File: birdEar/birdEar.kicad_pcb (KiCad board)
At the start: 2 copper layers, 96.5 x 88.9 mm, 59 parts, among them J1 Conn_01x03, J2 Micro_SD_Card_Det_Hirose_DM3AT, J3 SWD, J4 Conn_01x02_Male, J5 Conn_01x08_Male, J6 Conn_01x03_Male, SW2 KSA0A311 LFTR, SW3 KSA0A311 LFTR, SW4 KSA0A311 LFTR, U1 LM324, U2 AZ1117EH-3.3TRG1, U3 STM32F746ZGTx, U4 Si7050-A20, U5 LTR-303ALS-01

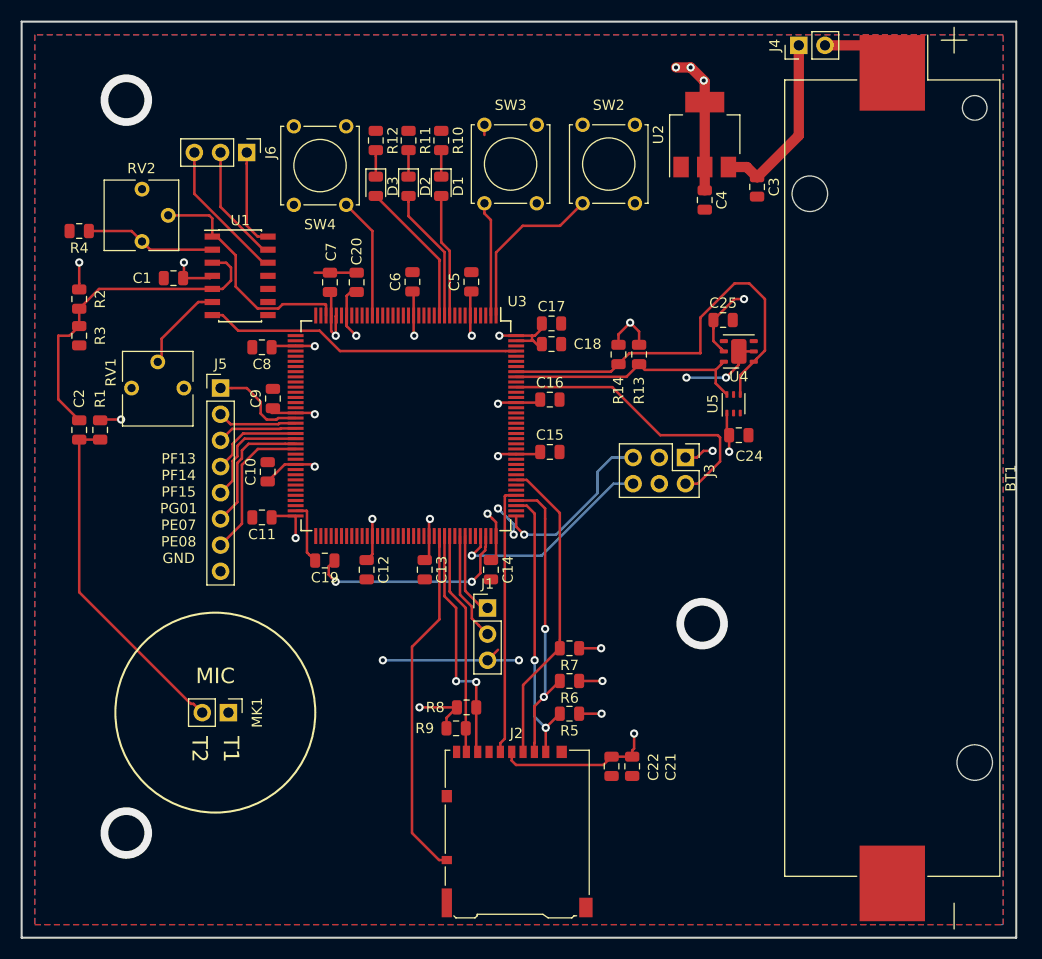
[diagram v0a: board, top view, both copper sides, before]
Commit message: Implemented anti aliasing filter, worked on the layout, added some gnd points
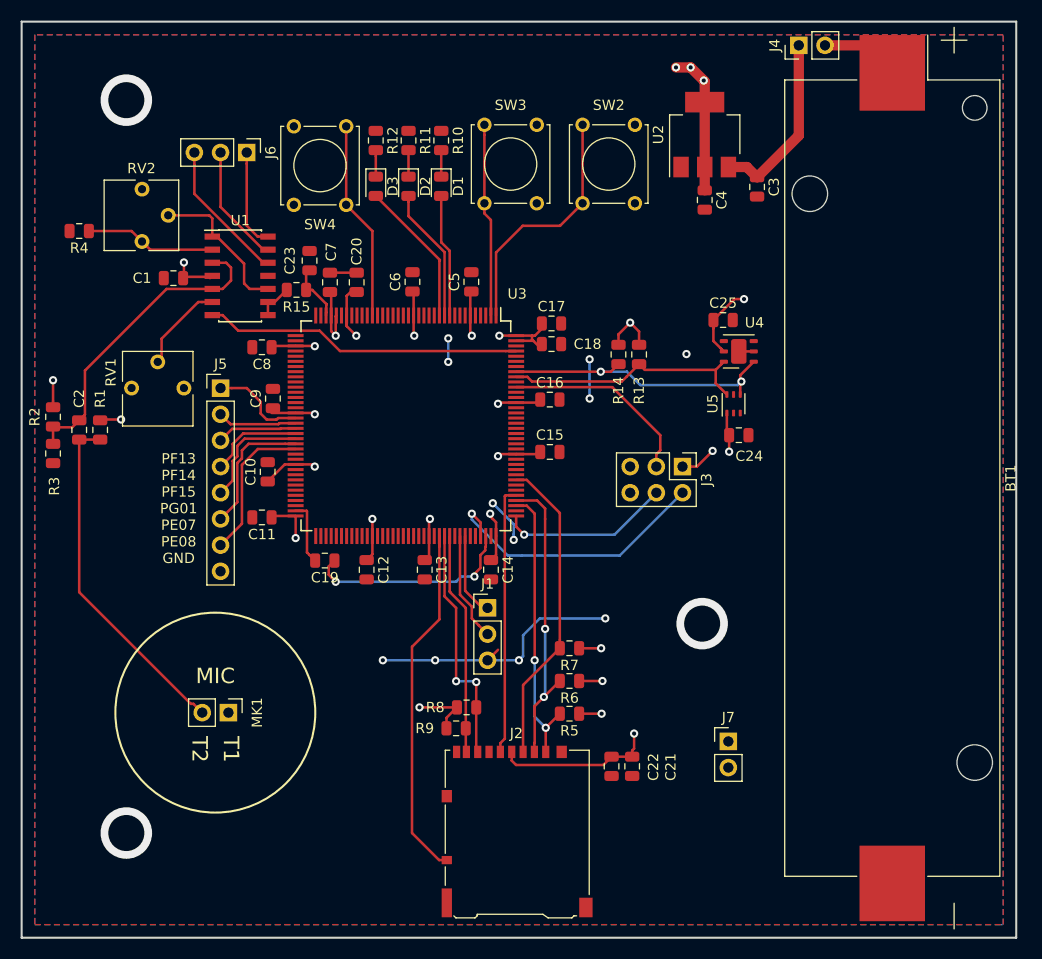
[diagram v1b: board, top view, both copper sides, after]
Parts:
- added C23: 1nF, Capacitor_SMD:C_0805_2012Metric, F.Cu at (94.0, 101.9)
- added J7: Conn_01x02_Male, Connector_PinHeader_2.54mm:PinHeader_1x02_P2.54mm_Vertical, F.Cu at (134.6, 148.6)
- added R15: 16k, Resistor_SMD:R_0805_2012Metric, F.Cu at (92.7, 104.8)
- J3: value SWD -> Conn_02x03_Odd_Even
- moved R3 11.7 mm to (69.1, 120.7)
- moved R2 11.7 mm to (69.1, 117.1)
- moved J3 0.92 mm to (130.2, 121.9)
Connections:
- J3 pad 2: /MCU/SW_RST -> /MCU/SWDIO
- J3 pad 3: GND -> /MCU/SW_RST
- J3 pad 4: Net-(J3-Pad4) -> /MCU/SWCLK
- J3 pad 5: /MCU/SWCLK -> GND
- J3 pad 6: /MCU/SWDIO -> Net-(J3-Pad6)
- RV2 pad 2: Audio -> Net-(RV2-Pad2)
- U1 pad 1: Audio -> Net-(RV2-Pad2)
- U1 pad 10: GND -> Net-(RV2-Pad2)
- U1 pad 8: Net-(U1-Pad8) -> Net-(R15-Pad2)
- U1 pad 9: GND -> Net-(R15-Pad2)
- U3 pad 34: Audio -> /MCU/Audio_In
- U4 pad 7: (no net) -> GND
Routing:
- net Audio: track 22.6 -> 0.00 mm
- net Net-(RV2-Pad2): track 0.00 -> 14.3 mm
- net /SCL: track 40.6 -> 28.3 mm, vias 0 -> 2
- net GND: track 29.9 -> 39.8 mm, vias 9 -> 14
- net /MCU/SW_RST: track 28.4 -> 19.1 mm
- net /PB1: track 16.5 -> 24.1 mm
- net Net-(SW4-Pad2): track 11.8 -> 19.4 mm
- net /MCU/SWDIO: track 20.8 -> 27.5 mm
- net /PB2: track 12.1 -> 18.8 mm
- net /MCU/Audio_In: track 0.00 -> 5.77 mm
- net Net-(R15-Pad2): track 0.00 -> 3.59 mm
- net /Raw_Audio: track 32.2 -> 30.6 mm
- net +3V3: track 139.4 -> 140.1 mm

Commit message: V1.0 of the PCB Complete
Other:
- board text added: "BIRD EAR V1.0 Ryan Walker, Jin Seo"
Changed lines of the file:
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@@
-(kicad_pcb (version 20171130) (host pcbnew 5.1.4-e60b266~84~ubuntu16.04.1)
+(kicad_pcb (version 20171130) (host pcbnew 5.0.2+dfsg1-1~bpo9+1)
   (general
     (thickness 1.6)
-    (drawings 9)
+    (drawings 10)
     (tracks 450)
     (zones 0)
@@
     (zone_45_only no)
     (trace_min 0.2)
+    (segment_width 0.2)
+    (edge_width 0.15)
     (via_size 0.8)
     (via_drill 0.4)
@@
     (uvia_min_size 0.2)
     (uvia_min_drill 0.1)
-    (edge_width 0.15)
-    (segment_width 0.2)
     (pcb_text_width 0.3)
     (pcb_text_size 1.5 1.5)
@@
     )
   )
+  (gr_text "BIRD EAR V1.0\nRyan Walker, Jin Seo" (at 92.964 161.036) (layer F.SilkS)
+    (effects (font (size 1.5 1.5) (thickness 0.3)))
+  )
   (gr_text "PF13\nPF14\nPF15\nPG01\nPE07\nPE08\nGND" (at 81.28 125.984) (layer F.SilkS)
     (effects (font (size 1 1) (thickness 0.25)))
@@
   (segment (start 79.623 109.509) (end 83.183 105.949) (width 0.25) (layer F.Cu) (net 16))
   (segment (start 79.623 111.154) (end 79.623 109.509) (width 0.25) (layer F.Cu) (net 16))
-  (segment (start 84.543 97.833) (end 84.543 99.599) (width 0.25) (layer F.Cu) (net 139))
-  (segment (start 84.25 97.54) (end 84.543 97.833) (width 0.25) (layer F.Cu) (net 139))
-  (segment (start 80.768 97.54) (end 84.25 97.54) (width 0.25) (layer F.Cu) (net 139))
   (segment (start 141.46 89.7925) (end 137.41 93.8425) (width 1) (layer F.Cu) (net 17))
   (segment (start 141.46 81.04) (end 141.46 89.7925) (width 1) (layer F.Cu) (net 17))
@@
   (segment (start 90.5985 105.949) (end 91.7725 104.775) (width 0.25) (layer F.Cu) (net 138))
   (segment (start 89.943 105.949) (end 90.5985 105.949) (width 0.25) (layer F.Cu) (net 138))
+  (segment (start 84.543 97.833) (end 84.543 99.599) (width 0.25) (layer F.Cu) (net 139))
+  (segment (start 84.25 97.54) (end 84.543 97.833) (width 0.25) (layer F.Cu) (net 139))
+  (segment (start 80.768 97.54) (end 84.25 97.54) (width 0.25) (layer F.Cu) (net 139))
   (segment (start 84.993 99.599) (end 87.63 102.236) (width 0.25) (layer F.Cu) (net 139))
   (segment (start 84.543 99.599) (end 84.993 99.599) (width 0.25) (layer F.Cu) (net 139))

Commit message: Generated BOM
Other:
- rule pad_to_mask_clearance: 0.051 -> 0.05
- rule solder_mask_min_width: 0.25 -> 0.05
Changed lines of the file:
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@@
   (page A4)
   (layers
-    (0 F.Cu signal)
-    (31 B.Cu signal)
-    (32 B.Adhes user)
-    (33 F.Adhes user)
-    (34 B.Paste user)
-    (35 F.Paste user)
+    (0 F.Cu signal hide)
+    (31 B.Cu signal hide)
+    (32 B.Adhes user hide)
+    (33 F.Adhes user hide)
+    (34 B.Paste user hide)
+    (35 F.Paste user hide)
     (36 B.SilkS user hide)
-    (37 F.SilkS user)
-    (38 B.Mask user)
+    (37 F.SilkS user hide)
+    (38 B.Mask user hide)
     (39 F.Mask user)
-    (40 Dwgs.User user)
-    (41 Cmts.User user)
-    (42 Eco1.User user)
-    (43 Eco2.User user)
-    (44 Edge.Cuts user)
-    (45 Margin user)
-    (46 B.CrtYd user)
-    (47 F.CrtYd user)
+    (40 Dwgs.User user hide)
+    (41 Cmts.User user hide)
+    (42 Eco1.User user hide)
+    (43 Eco2.User user hide)
+    (44 Edge.Cuts user hide)
+    (45 Margin user hide)
+    (46 B.CrtYd user hide)
+    (47 F.CrtYd user hide)
     (48 B.Fab user hide)
     (49 F.Fab user hide)
@@
     (pad_size 1.5 2.4)
     (pad_drill 0)
-    (pad_to_mask_clearance 0.051)
-    (solder_mask_min_width 0.25)
+    (pad_to_mask_clearance 0.05)
+    (solder_mask_min_width 0.05)
     (aux_axis_origin 0 0)
     (visible_elements FFFFFF7F)
@@
       (drillshape 0)
       (scaleselection 1)
-      (outputdirectory "gerb/"))
+      (outputdirectory "gerb/drl/"))
   )
   (net 0 "")
